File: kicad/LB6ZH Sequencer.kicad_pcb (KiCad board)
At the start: 2 copper layers, 160 x 100 mm, 100 parts, among them J1 1x2, J10 Conn_01x03, J11 1x3, J12 RCA, J14 Conn_01x02, J15 Conn_01x02, J16 Conn_01x02, J17 Conn_01x02, J18 Conn_01x02, J19 Conn_01x02, J2 Screw_Terminal_01x02, J20 Conn_01x02, J21 Conn_01x02, J22 Conn_01x02, J23 1x3, J24 1x3, J25 1x3, J26 1x3, J27 1x3, J28 1x3, J29 Conn_01x02, J3 Conn_01x02, J30 Conn_01x02, J31 Conn_01x02, J32 Conn_01x02, J33 Conn_01x02, J34 Conn_01x02, J35 Conn_01x02, J36 Conn_01x02, J37 Conn_01x02, J38 Conn_01x02, J39 Conn_01x02, J4 Conn_01x02, J40 Conn_01x02, J41 1x3, J42 1x3, J43 1x3, J44 1x3, J45 Conn_01x02, J46 Conn_01x02, J47 Conn_01x02, J48 Conn_01x02, J5 Conn_01x02, J6 Conn_01x02, J7 Conn_01x02, J8 Conn_01x02, J9 Conn_01x02, K1 FINDER-30.22, K2 FINDER-30.22, K3 FINDER-30.22, K4 FINDER-30.22, K5 FINDER-30.22, SW1 SW_DPDT_x2, U1 PC817, U2 PC817, U3 PC817, U4 PC817, U5 PC817, U6 PC817

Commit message: Updates to kicad PCB after prototype assembly.
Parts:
- removed C11, C9: 10n, Capacitor_THT:C_Rect_L4.6mm_W2.0mm_P2.50mm_MKS02_FKP02
- removed D15: 1N4001, Diode_THT:D_DO-41_SOD81_P10.16mm_Horizontal
- removed J35, J37, J38, J45, J46: Conn_01x02, Connector_PinHeader_2.54mm:PinHeader_1x02_P2.54mm_Vertical
- removed J41, J43: 1x3, TerminalBlock_Phoenix:TerminalBlock_Phoenix_MKDS-3-3-5.08_1x03_P5.08mm_Horizontal
- removed K4: FINDER-30.22, Relay_THT:Relay_DPDT_Finder_30.22
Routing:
- net GND: track 3064.3 -> 1057.7 mm, vias 190 -> 46
- net VIN: track 152.8 -> 422.0 mm, vias 2 -> 17
- net unconnected-(A1-D8-Pad11): track 20.3 -> 0.00 mm
- net Net-(D3-K): track 20.3 -> 2.54 mm
- net Net-(J26-Pin_2): track 12.7 -> 0.00 mm
- net OC_PREAMP: track 28.0 -> 15.3 mm, vias 0 -> 1
- net Net-(J17-Pin_2): track 12.7 -> 0.01 mm
- net Net-(J44-Pin_2): track 12.7 -> 0.00 mm
- net Net-(J28-Pin_2): track 12.7 -> 0.00 mm
- net unconnected-(A1-MISO-Pad15): track 12.7 -> 0.00 mm
- net PA_PTT: track 35.6 -> 22.9 mm
- net Net-(R7-Pad1): track 35.6 -> 22.9 mm
- net Net-(J27-Pin_2): track 12.7 -> 0.00 mm
- net Net-(D4-K): track 15.2 -> 2.54 mm
- net Net-(A1-D10): track 62.0 -> 49.3 mm
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
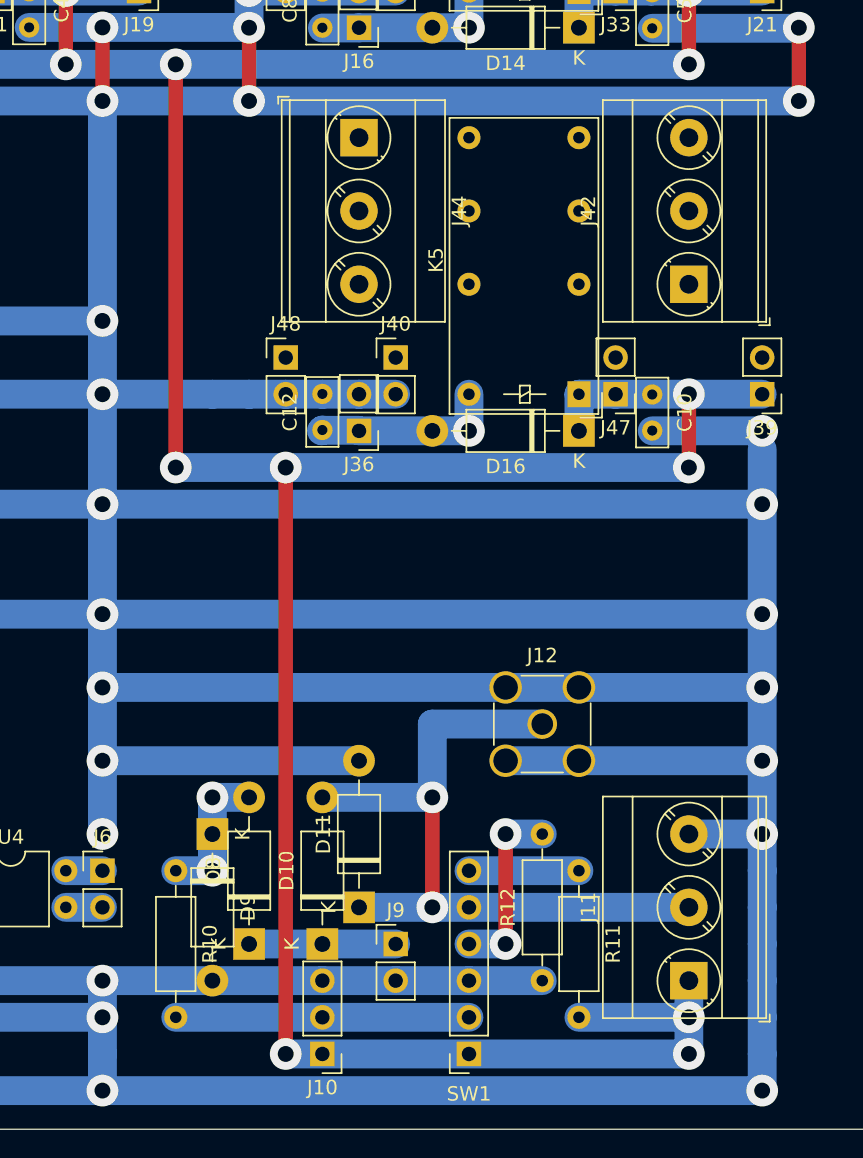
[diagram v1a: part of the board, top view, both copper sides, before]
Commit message: Fixed a net that was grounded in error.
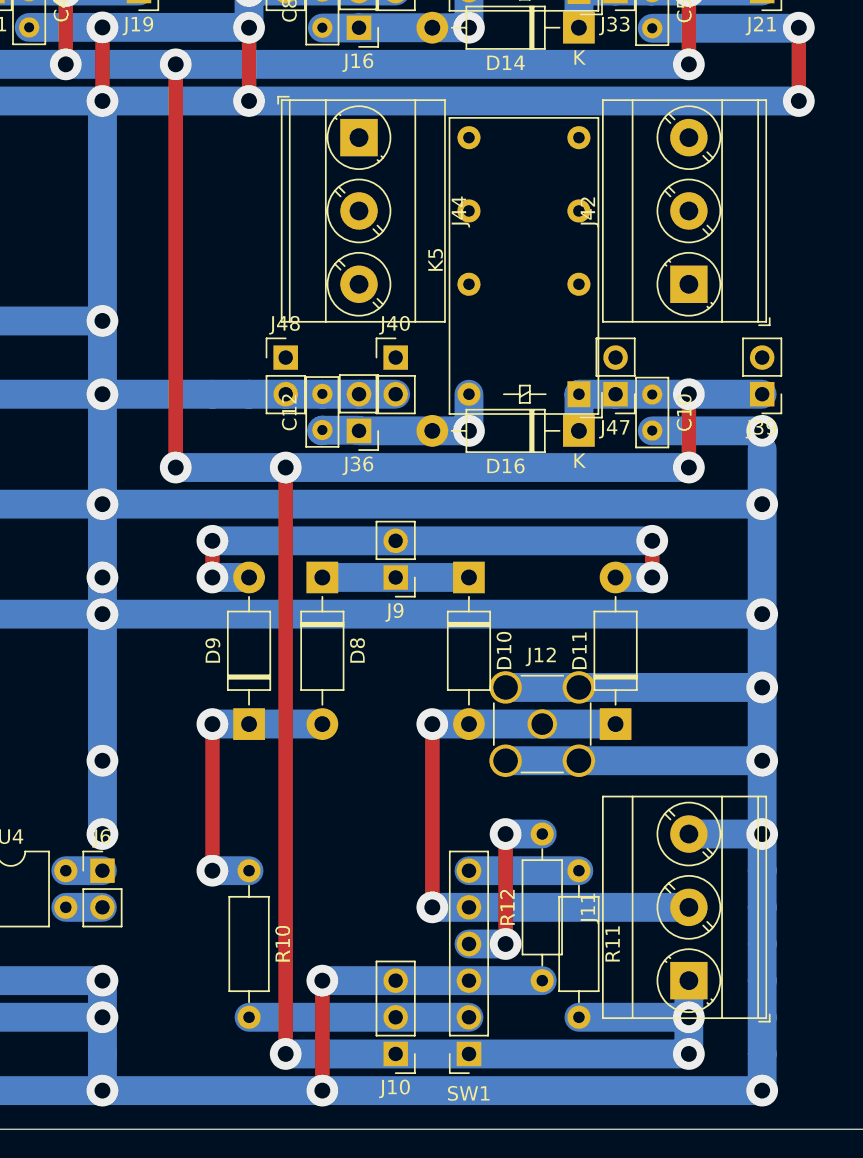
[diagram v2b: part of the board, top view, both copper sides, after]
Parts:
- moved D10 27.4 mm to (172.7, 111.8), turned to -90 degrees
- moved D8 25.9 mm to (162.6, 111.8), turned to -90 degrees
- moved J9 25.4 mm to (167.6, 111.8), turned to 180 degrees
- moved D11 21.8 mm to (182.9, 121.9)
- moved D9 8.03 mm to (157.5, 121.9), turned to 90 degrees
- moved J10 5.08 mm to (167.6, 144.8)
- moved R10 5.08 mm to (157.5, 132.1)
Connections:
- D11 pad 2: GND -> Net-(D11-A)
- D9 pad 2: GND -> Net-(D11-A)
- J9 pad 2: GND -> Net-(D11-A)
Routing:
- net GND: track 1057.7 -> 1004.4 mm, vias 46 -> 48
- net Net-(D11-A): track 0.00 -> 40.6 mm, vias 0 -> 4
- net Net-(D8-A): track 10.2 -> 20.3 mm
- net Net-(D10-A): track 50.8 -> 43.2 mm
- net Net-(J10-Pin_2): track 20.3 -> 15.2 mm

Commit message: Minor corrections after applying mods on prototype.
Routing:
- net GND: track 1004.4 -> 1118.7 mm, vias 48 -> 51
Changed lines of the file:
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@@
   (gr_rect (start 107.95 95.25) (end 110.49 97.79)
     (stroke (width 0.1) (type default)) (fill none) (layer "User.4"))
+  (gr_rect (start 148.59 140.97) (end 151.13 143.51)
+    (stroke (width 0.1) (type default)) (fill none) (layer "User.4"))
   (gr_rect (start 100.33 67.31) (end 102.87 69.85)
+    (stroke (width 0.1) (type default)) (fill none) (layer "User.4"))
+  (gr_rect (start 148.59 120.65) (end 151.13 123.19)
     (stroke (width 0.1) (type default)) (fill none) (layer "User.4"))
   (gr_rect (start 148.59 107.95) (end 151.13 113.03)
@@
   (gr_rect (start 181.61 100.33) (end 184.15 102.87)
     (stroke (width 0.1) (type default)) (fill none) (layer "User.4"))
-  (gr_rect (start 148.59 115.57) (end 151.13 146.05)
+  (gr_rect (start 148.59 125.73) (end 151.13 138.43)
     (stroke (width 0.1) (type default)) (fill none) (layer "User.4"))
   (gr_rect (start 59.69 110.49) (end 62.23 113.03)
@@
   (segment (start 195.58 78.74) (end 195.58 73.66) (width 1) (layer "F.Cu") (net 4))
   (segment (start 147.32 78.74) (end 147.32 73.64) (width 1) (layer "F.Cu") (net 4))
+  (segment (start 152.4 124.46) (end 152.4 139.7) (width 1) (layer "F.Cu") (net 4))
   (segment (start 157.48 78.74) (end 157.48 73.66) (width 1) (layer "F.Cu") (net 4))
   (segment (start 60.96 78.74) (end 60.96 71.12) (width 1) (layer "F.Cu") (net 4))
   (segment (start 114.3 78.74) (end 114.3 73.66) (width 1) (layer "F.Cu") (net 4))
   (segment (start 114.3 73.66) (end 114.285 73.645) (width 1) (layer "F.Cu") (net 4))
-  (segment (start 162.56 147.32) (end 162.56 139.7) (width 1) (layer "F.Cu") (net 4))
   (segment (start 71.12 99.06) (end 71.12 93.98) (width 1) (layer "F.Cu") (net 4))
   (via (at 157.48 78.74) (size 2.2) (drill 1.1) (layers "F.Cu" "B.Cu") (net 4))
@@
   (via (at 193.04 147.32) (size 2.2) (drill 1.1) (layers "F.Cu" "B.Cu") (net 4))
   (via (at 147.32 111.76) (size 2.2) (drill 1.1) (layers "F.Cu" "B.Cu") (net 4))
+  (via (at 147.32 116.84) (size 2.2) (drill 1.1) (layers "F.Cu" "B.Cu") (net 4))
   (via (at 147.32 93.98) (size 2.2) (drill 1.1) (layers "F.Cu" "B.Cu") (net 4))
   (via (at 58.42 109.22) (size 2.2) (drill 1.1) (layers "F.Cu" "B.Cu") (net 4))
@@
   (via (at 66.04 109.22) (size 2.2) (drill 1.1) (layers "F.Cu" "B.Cu") (net 4))
   (via (at 147.32 106.68) (size 2.2) (drill 1.1) (layers "F.Cu" "B.Cu") (net 4))
+  (via (at 147.32 119.38) (size 2.2) (drill 1.1) (layers "F.Cu" "B.Cu") (net 4))
   (via (at 193.04 124.46) (size 2.2) (drill 1.1) (layers "F.Cu" "B.Cu") (net 4))
   (via (at 147.32 99.06) (size 2.2) (drill 1.1) (layers "F.Cu" "B.Cu") (net 4))
+  (via (at 193.04 116.84) (size 2.2) (drill 1.1) (layers "F.Cu" "B.Cu") (net 4))
   (via (at 111.76 106.68) (size 2.2) (drill 1.1) (layers "F.Cu" "B.Cu") (net 4))
   (via (at 114.3 78.74) (size 2.2) (drill 1.1) (layers "F.Cu" "B.Cu") (net 4))
@@
   (via (at 157.48 71.12) (size 2.2) (drill 1.1) (layers "F.Cu" "B.Cu") (net 4))
   (via (at 121.92 139.7) (size 2.2) (drill 1.1) (layers "F.Cu" "B.Cu") (net 4))
-  (via (at 162.56 147.32) (size 2.2) (drill 1.1) (layers "F.Cu" "B.Cu") (net 4))
   (via (at 137.16 147.32) (size 2.2) (drill 1.1) (layers "F.Cu" "B.Cu") (net 4))
+  (via (at 152.4 124.46) (size 2.2) (drill 1.1) (layers "F.Cu" "B.Cu") (net 4))
   (via (at 147.32 78.74) (size 2.2) (drill 1.1) (layers "F.Cu" "B.Cu") (net 4))
-  (via (at 162.56 139.7) (size 2.2) (drill 1.1) (layers "F.Cu" "B.Cu") (net 4))
   (via (at 157.48 73.66) (size 2.2) (drill 1.1) (layers "F.Cu" "B.Cu") (net 4))
   (via (at 60.96 78.74) (size 2.2) (drill 1.1) (layers "F.Cu" "B.Cu") (net 4))
@@
   (via (at 60.96 71.12) (size 2.2) (drill 1.1) (layers "F.Cu" "B.Cu") (net 4))
   (via (at 106.68 142.24) (size 2.2) (drill 1.1) (layers "F.Cu" "B.Cu") (net 4))
+  (via (at 152.4 139.7) (size 2.2) (drill 1.1) (layers "F.Cu" "B.Cu") (net 4))
   (via (at 137.16 139.7) (size 2.2) (drill 1.1) (layers "F.Cu" "B.Cu") (net 4))
   (via (at 71.12 104.14) (size 2.2) (drill 1.1) (layers "F.Cu" "B.Cu") (net 4))
@@
   (segment (start 157.48 78.74) (end 60.96 78.74) (width 2) (layer "B.Cu") (net 4))
   (segment (start 147.32 111.76) (end 147.32 78.74) (width 2) (layer "B.Cu") (net 4))
+  (segment (start 193.04 119.38) (end 147.32 119.38) (width 2) (layer "B.Cu") (net 4))
   (segment (start 106.68 147.32) (end 106.68 142.24) (width 2) (layer "B.Cu") (net 4))
   (segment (start 154.94 99.06) (end 157.48 99.06) (width 2) (layer "B.Cu") (net 4))
@@
   (segment (start 121.92 147.32) (end 121.92 139.7) (width 2) (layer "B.Cu") (net 4))
   (segment (start 165.1 99.06) (end 167.64 99.06) (width 2) (layer "B.Cu") (net 4))
+  (segment (start 147.32 124.46) (end 165.1 124.46) (width 2) (layer "B.Cu") (net 4))
   (segment (start 157.48 71.12) (end 157.48 73.66) (width 2) (layer "B.Cu") (net 4))
   (segment (start 86.36 127) (end 86.36 129.54) (width 2) (layer "B.Cu") (net 4))
@@
   (segment (start 72.45 132.08) (end 72.39 132.14) (width 0.2) (layer "B.Cu") (net 4))
   (segment (start 106.68 142.24) (end 106.68 139.7) (width 2) (layer "B.Cu") (net 4))
-  (segment (start 193.04 119.38) (end 175.26 119.38) (width 2) (layer "B.Cu") (net 4))
   (segment (start 160.02 99.06) (end 162.56 99.06) (width 2) (layer "B.Cu") (net 4))
   (segment (start 121.92 114.3) (end 147.32 114.3) (width 2) (layer "B.Cu") (net 4))
@@
   (segment (start 193.04 142.24) (end 193.04 144.78) (width 2) (layer "B.Cu") (net 4))
   (segment (start 68.585 71.125) (end 68.58 71.12) (width 0.2) (layer "B.Cu") (net 4))
+  (segment (start 147.32 116.84) (end 193.04 116.84) (width 2) (layer "B.Cu") (net 4))
   (segment (start 137.16 147.32) (end 137.16 144.78) (width 2) (layer "B.Cu") (net 4))
   (segment (start 157.46 73.64) (end 157.48 73.66) (width 2) (layer "B.Cu") (net 4))
@@
   (segment (start 193.04 129.54) (end 193.04 132.08) (width 2) (layer "B.Cu") (net 4))
   (segment (start 193.04 129.54) (end 193.04 102.87) (width 2) (layer "B.Cu") (net 4))
+  (segment (start 177.8 139.7) (end 147.32 139.7) (width 2) (layer "B.Cu") (net 4))
   (segment (start 147.32 147.32) (end 137.16 147.32) (width 2) (layer "B.Cu") (net 4))
-  (segment (start 177.8 139.7) (end 162.56 139.7) (width 2) (layer "B.Cu") (net 4))
   (segment (start 137.16 139.7) (end 137.16 137.16) (width 2) (layer "B.Cu") (net 4))
   (segment (start 111.76 106.68) (end 147.32 106.68) (width 2) (layer "B.Cu") (net 4))
